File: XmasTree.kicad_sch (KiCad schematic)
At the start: 18 parts, among them J1 USB_B_Micro, Q1 BSN20, SW1 SW_Push, SW2 SW_Push, SW3 SW_Push, SW4 SW_Push, U1 FT231XQ, U2 AP2202K-3.3

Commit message: Swap FT231XQ for FT231XS
Signed-off-by: Giuseppe Barillari <joe2k01dev@gmail.com>
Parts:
- removed U1: FT231XQ, Package_DFN_QFN:QFN-20-1EP_4x4mm_P0.5mm_EP2.5x2.5mm, symbol Interface_USB:FT231XQ
- added U1: FT231XS, Package_SO:SSOP-20_3.9x8.7mm_P0.635mm, symbol Interface_USB:FT231XS
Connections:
- net +5V: now also U1.15 (VCC)
- net 3v3 MCU/UartRX: now also U1.20 (TXD)
- net 3v3 MCU/UartTX: now also U1.4 (RXD)
- net GND: now also U1.16 (GND), U1.6 (GND)
- net UsbD+: now also U1.11 (USBDP)
- net UsbD-: now also U1.12 (USBDM)
- net at R1.2: now also U1.14 (~{RESET})
- new net: U1.13 (3V3OUT), U1.3 (VCCIO)
- no-connect marks 0 -> 11

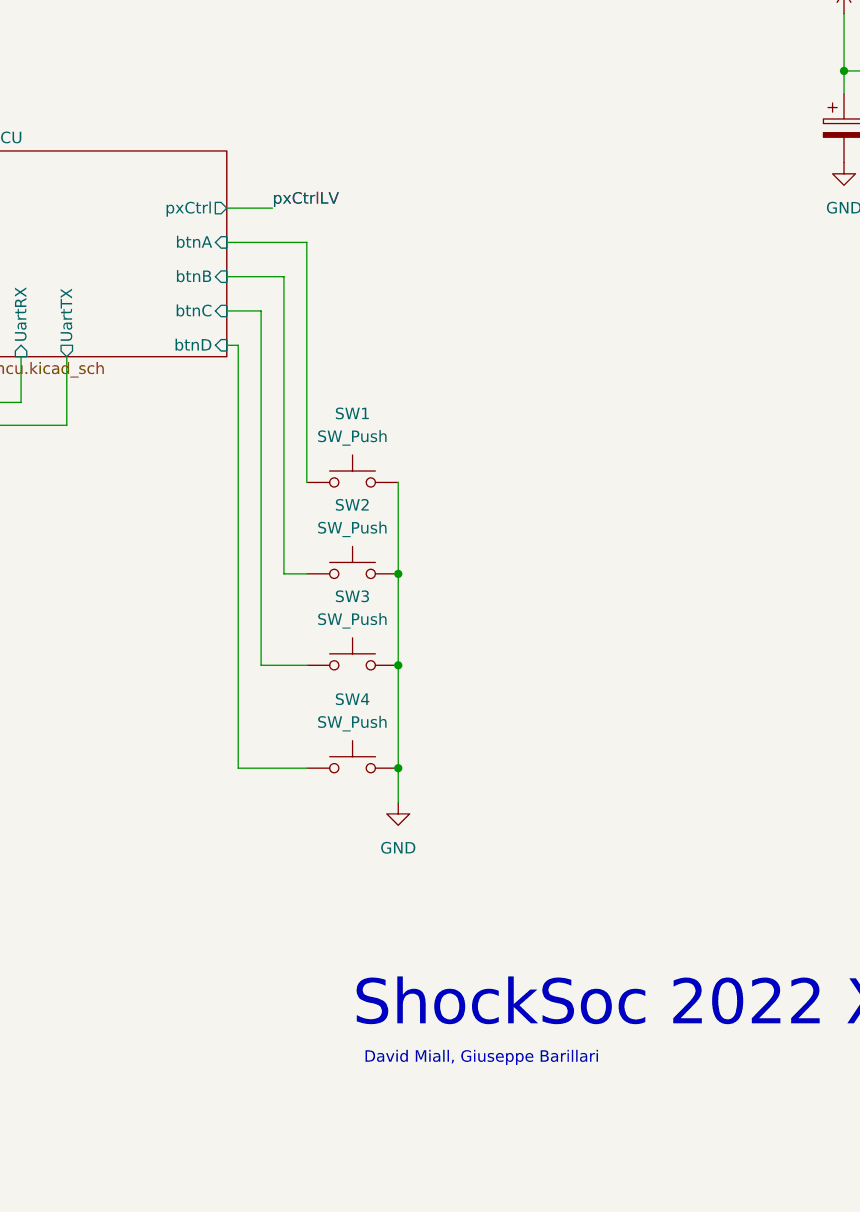
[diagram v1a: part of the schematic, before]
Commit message: Start laying out pcb
Signed-off-by: Giuseppe Barillari <joe2k01dev@gmail.com>
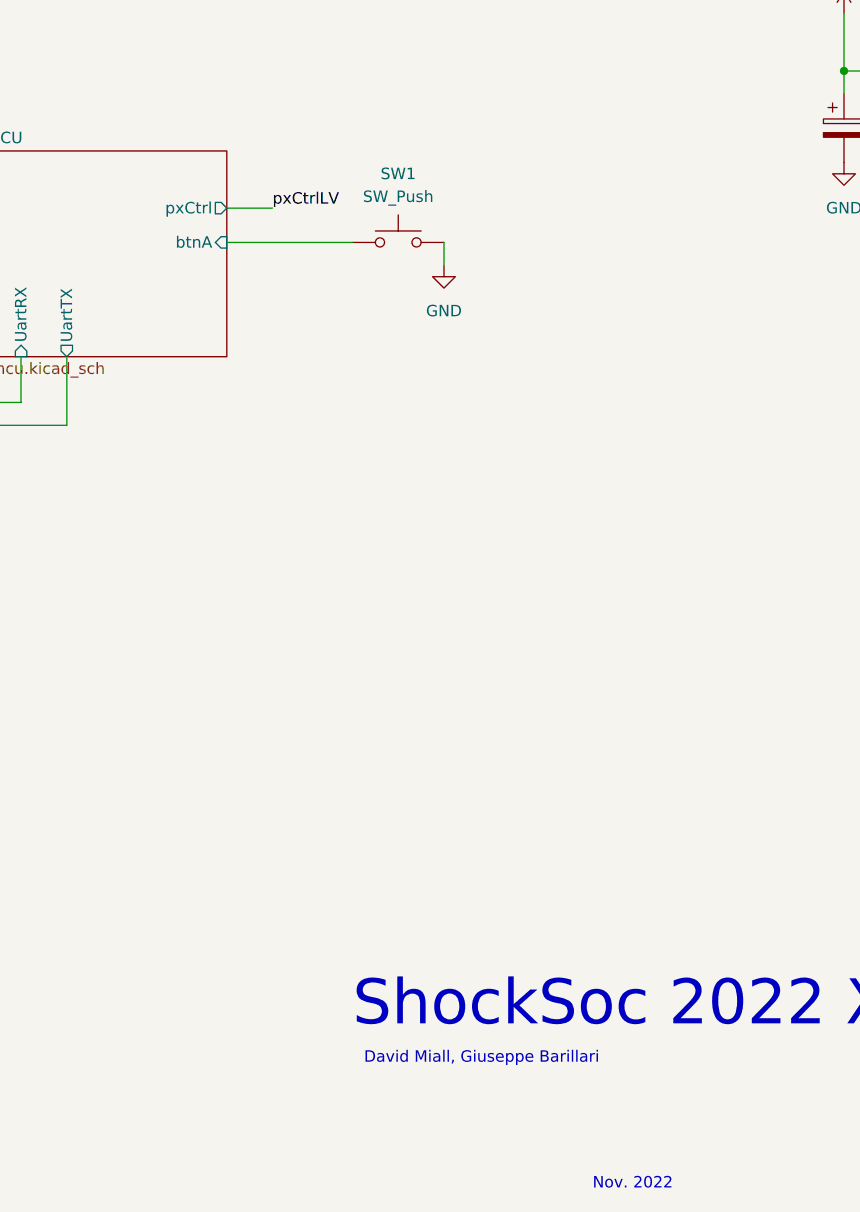
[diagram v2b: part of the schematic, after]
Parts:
- removed SW2, SW3, SW4: SW_Push, Button_Switch_SMD:SW_Push_1P1T_NO_6x6mm_H9.5mm, symbol Switch:SW_Push
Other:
- sheet 3v3 MCU ports: added none; removed btnB, btnC, btnD
- note added: "Nov. 2022"
- moved on the sheet: SW1
